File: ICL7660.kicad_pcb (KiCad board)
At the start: 2 copper layers, 38.1 x 31.8 mm, 14 parts, among them J1 Vin, J2 GND, J3 Vout, J4 GND, J5 -Vout, U1 ICL7660

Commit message: 配置を修正
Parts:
- removed the J4 at (154.9, 95.0)
- added H1: MountingHole, MountingHole:MountingHole_3.2mm_M3, F.Cu at (118.7, 61.2)
- added H2: MountingHole, MountingHole:MountingHole_3.2mm_M3, F.Cu at (146.7, 68.8)
- C1, C5: footprint Capacitor_THT:CP_Radial_D6.3mm_P2.50mm -> Capacitor_THT:CP_Radial_D10.0mm_P2.50mm
- R1, R2: footprint Resistor_THT:R_Axial_DIN0204_L3.6mm_D1.6mm_P7.62mm_Horizontal -> Resistor_THT:R_Axial_DIN0204_L3.6mm_D1.6mm_P2.54mm_Vertical
- moved J1 26.2 mm to (127.4, 68.4), turned to 90 degrees
- moved R1 24.1 mm to (130.6, 71.4), turned to 90 degrees
- moved R2 23.8 mm to (123.8, 61.5)
- moved J2 22.1 mm to (127.4, 72.3), turned to 90 degrees
- moved J3 21.6 mm to (133.8, 77.9), turned to 90 degrees
- moved C2 20.3 mm to (133.8, 74.1)
- moved C6 17.5 mm to (123.4, 68.0)
- moved C5 15.1 mm to (120.5, 77.8), turned to 0 degrees
- moved C4 15.0 mm to (128.7, 63.8), turned to 90 degrees
- moved J4 14.9 mm to (129.2, 77.9), turned to 90 degrees
- moved C1 14.7 mm to (143.1, 76.3), turned to -90 degrees
- moved C3 11.3 mm to (146.7, 62.3), turned to 90 degrees
- moved U1 7.60 mm to (141.4, 68.9), turned to 180 degrees
- renumbered J5 to J4
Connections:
- C5 pad 1: Net-(J5-Pin_1) -> GND
- C5 pad 2: GND -> Net-(J4-Pin_1)
- C6 pad 1: Net-(J5-Pin_1) -> Net-(J4-Pin_1)
- J4 pad 1: Net-(J5-Pin_1) -> Net-(J4-Pin_1)
- R2 pad 2: Net-(J5-Pin_1) -> Net-(J4-Pin_1)
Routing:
- net GND: track 68.1 -> 0.00 mm
- net Net-(J4-Pin_1): track 0.00 -> 20.3 mm
- net Net-(J5-Pin_1): track 14.4 -> 0.00 mm
- net Net-(J1-Pin_1): track 9.63 -> 5.10 mm
- net Net-(J3-Pin_1): track 22.4 -> 19.1 mm
- net Net-(U1-CAP+): track 5.64 -> 7.04 mm
- net Net-(U1-VOUT): track 9.43 -> 10.2 mm
- added copper zone on B.Cu, net GND
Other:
- board size 38.1 x 31.8 mm -> 35.2 x 25.7 mm

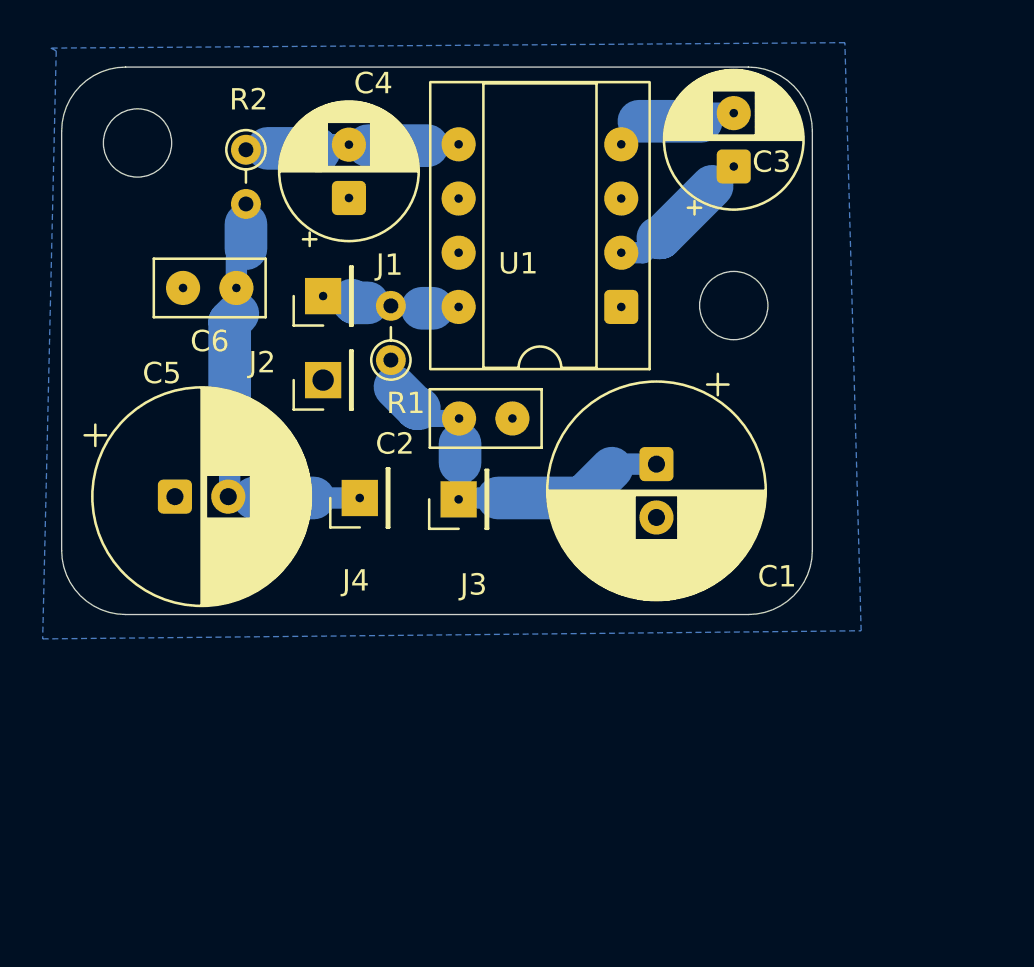
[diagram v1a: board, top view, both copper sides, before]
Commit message: LED用の抵抗を追加
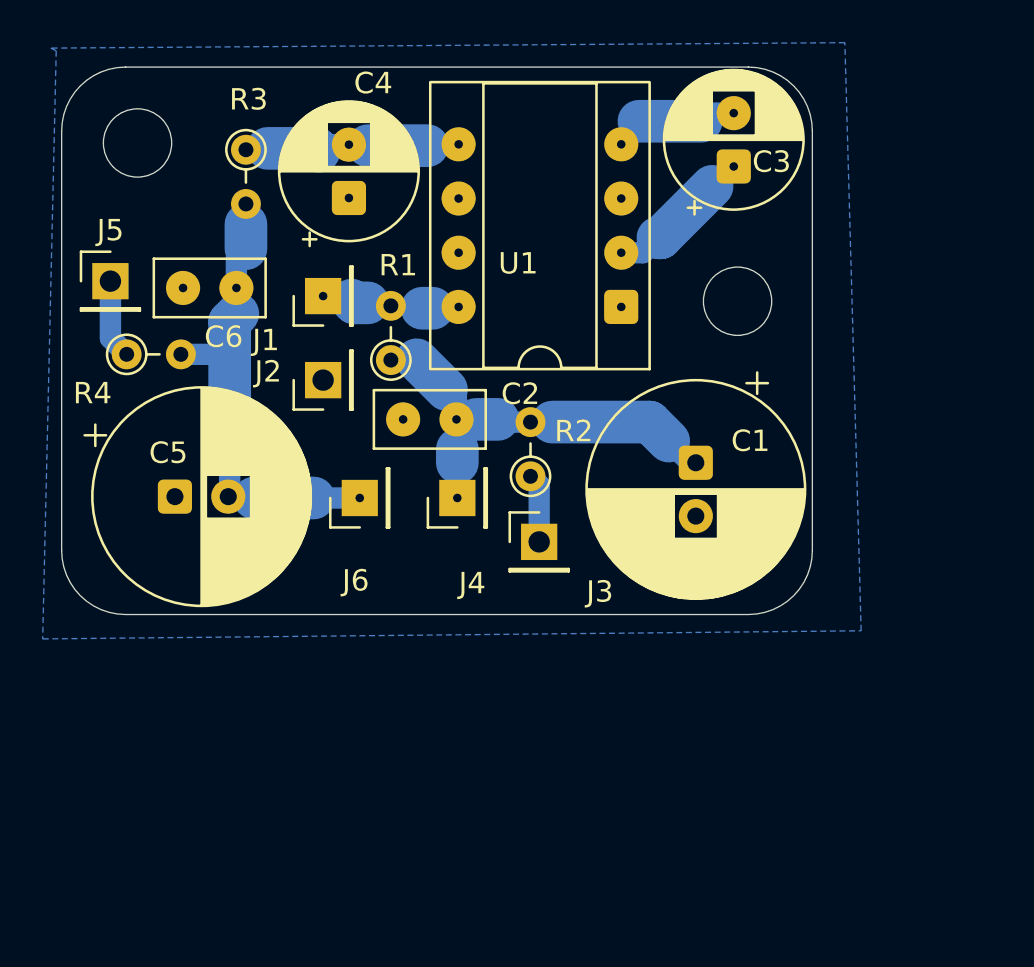
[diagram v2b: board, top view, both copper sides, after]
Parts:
- added J3: +Led, Connector_PinHeader_2.54mm:PinHeader_1x01_P2.54mm_Vertical, F.Cu at (137.6, 79.9)
- added J5: +Led, Connector_PinHeader_2.54mm:PinHeader_1x01_P2.54mm_Vertical, F.Cu at (117.5, 67.7)
- added R2: 2.2k, Resistor_THT:R_Axial_DIN0204_L3.6mm_D1.6mm_P2.54mm_Vertical, F.Cu at (137.2, 76.8)
- added R4: 2.2k, Resistor_THT:R_Axial_DIN0204_L3.6mm_D1.6mm_P2.54mm_Vertical, F.Cu at (118.2, 71.1)
- moved C1 1.85 mm to (144.9, 76.2)
- moved H2 0.27 mm to (146.9, 68.6)
- moved C2 0.13 mm to (133.7, 74.2), turned to 180 degrees
- moved J4 0.09 mm to (133.7, 77.9)
- renumbered J3 to J4, J4 to J6, R2 to R3
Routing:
- net Net-(D2-K): track 0.00 -> 3.74 mm
- net Net-(D1-A): track 0.00 -> 3.24 mm
- net Net-(J6-Pin_1): track 20.3 -> 22.7 mm
- net Net-(J4-Pin_1): track 19.1 -> 20.5 mm
